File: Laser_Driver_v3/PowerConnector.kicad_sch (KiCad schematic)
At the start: 1 part, among them J2 Conn_02x12_Counter_Clockwise

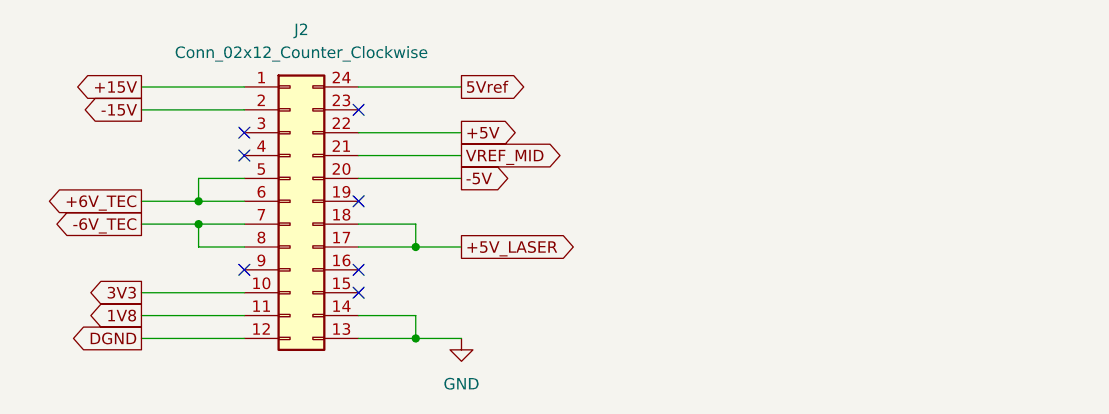
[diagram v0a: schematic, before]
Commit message: Power PCB lay out done with no DRC errors.
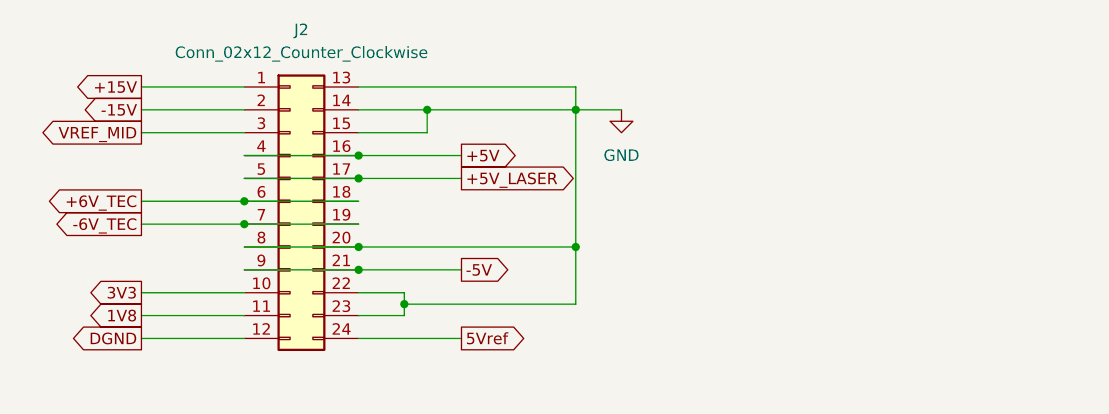
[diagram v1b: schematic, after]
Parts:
- J2: symbol Connector_Generic:Conn_02x12_Counter_Clockwise -> Connector_Generic:Conn_02x12_Top_Bottom
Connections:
- net +5V: now also J2.16 (Pin_16), J2.4 (Pin_4); no longer J2.22 (Pin_22)
- net +5V_LASER: now also J2.5 (Pin_5); no longer J2.18 (Pin_18)
- net +6V_TEC: now also J2.18 (Pin_18); no longer J2.5 (Pin_5)
- net -5V: now also J2.21 (Pin_21), J2.9 (Pin_9); no longer J2.20 (Pin_20)
- net -6V_TEC: now also J2.19 (Pin_19); no longer J2.8 (Pin_8)
- net GND: now also J2.15 (Pin_15), J2.20 (Pin_20), J2.22 (Pin_22), J2.23 (Pin_23), J2.8 (Pin_8)
- net VREF_MID: now also J2.3 (Pin_3); no longer J2.21 (Pin_21)
- no-connect marks 7 -> 0

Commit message: updated to newer/available parts
Routing needs to be completely redone.
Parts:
- renumbered J2 to J6
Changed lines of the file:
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@@
 		(dnp no)
 		(fields_autoplaced yes)
-		(property "Reference" "J2"
+		(property "Reference" "J6"
 			(at 88.9 48.26 0)
 			(show_name no)
@@
 			(project "laser_driver_v3_Power"
 				(path "/b2c3d4e5-f6a7-8901-bcde-f12345678901/95c9f2bc-5f61-41c2-a204-afd07f26a3be"
-					(reference "J2")
+					(reference "J6")
 					(unit 1)
 				)

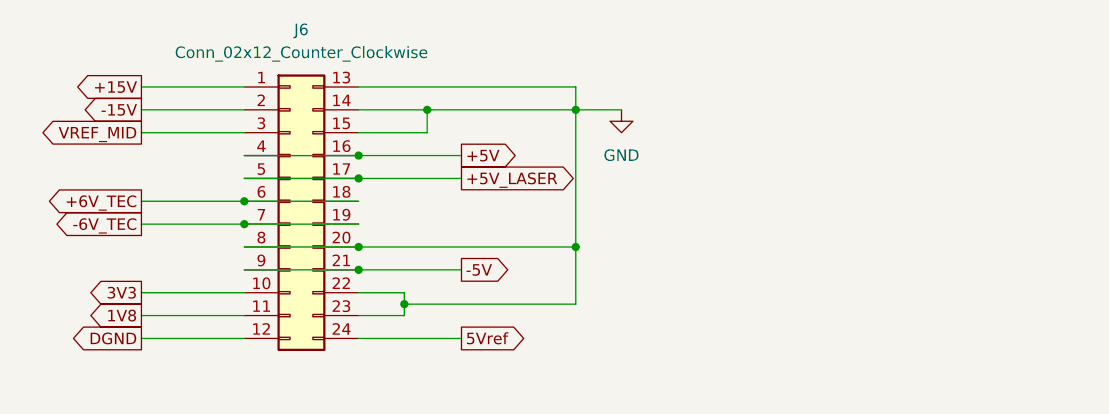
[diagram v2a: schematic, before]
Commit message: Added NTC for heatsink.  orrected screw terminal#s
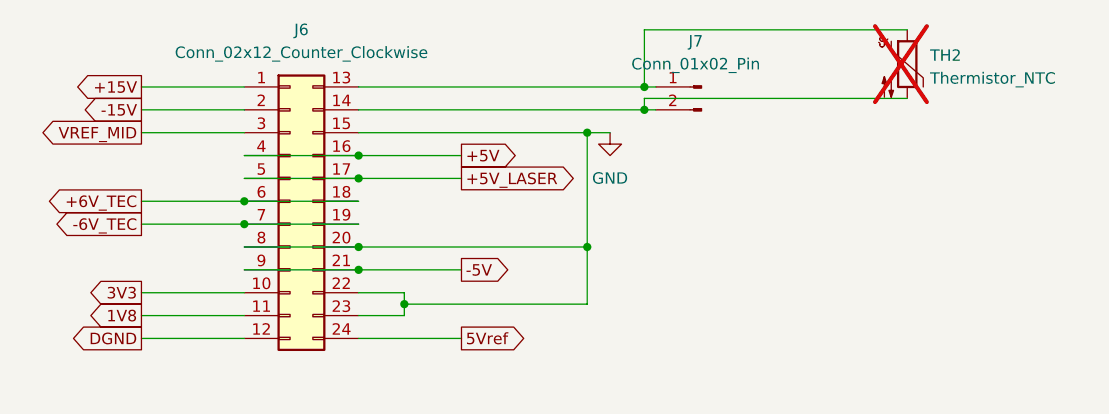
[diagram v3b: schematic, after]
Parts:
- added J7: Conn_01x02_Pin, Connector_Phoenix_MSTB:PhoenixContact_MSTBA_2,5_2-G_1x02_P5.00mm_Horizontal, symbol Connector:Conn_01x02_Pin
- added TH2: Thermistor_NTC, symbol Device:Thermistor_NTC
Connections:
- net GND: no longer J6.13 (Pin_13), J6.14 (Pin_14)
- new net: J6.13 (Pin_13), J7.1 (Pin_1), TH2.1
- new net: J6.14 (Pin_14), J7.2 (Pin_2), TH2.2
